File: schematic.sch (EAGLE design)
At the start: 31 parts, among them IC1 FT230XS, IC2 ATMEGA644A, IC4 L4931D, X1 MINI-USB-32005-301

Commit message: saving to git
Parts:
- added C11: .1uf, eagle-ltspice:CC0504
- added C12, C13, C17: 1uF, eagle-ltspice:CC0504
- added C14, C15: 2.2uF, eagle-ltspice:CC0504
- added C16: .1uF, eagle-ltspice:CC0504
- added R12, R13: 2K, eagle-ltspice:RR0603
- added R14: 390K, eagle-ltspice:RR0603
- added U$3: UG-2864HSWEG01, adafruit:UG-2864HSWEG01
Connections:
- new net N$10: C13.1, U$3.C2N
- new net N$11: C17.2, U$3.C1P
- new net N$12: C17.1, U$3.C1N
- new net N$5: C14.2, U$3.VCOMH
- new net N$7: C13.2, U$3.C2P
- new net N$9: R14.1, U$3.IREF
- new net OLED_SCL: R12.1, U$3.D0/DI
- new net OLED_SDA: R13.1, U$3.D1/SCLK, U$3.D2
- new net OLED_VCC: C15.2, C16.2, U$3.VCC
- new net OLED_VDD: C11.2, C12.2, R12.2, R13.2, U$3./RES, U$3.BS1, U$3.VBAT, U$3.VDD
- new net OLED_VSS: U$3./CS, U$3.BS0, U$3.BS2, U$3.R/W
- net GND: now also C11.1, C12.1, C14.1, C15.1, C16.1, R14.2, U$3.D/C, U$3.E/RD, U$3.VLSS, U$3.VSS
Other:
- moved on the sheet: X1

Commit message: saving
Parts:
- removed IC2: ATMEGA644A, atmel:ATMEGA644A
- added C18: 1uF, eagle-ltspice:CC0504
- added IC3: ATMEGA32U2-TQFP, adafruit:ATMEGA32U2-TQFP
- added JP1: (no value), adafruit:PINHD-1X6B
- added R15, R16: 22, eagle-ltspice:RR0603
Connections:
- new net N$13: IC3.PB3(PDO/MISO/PCINT3), JP1.4
- new net N$14: C18.2, IC3.UCAP
- new net N$15: IC3.D-, R15.1
- new net N$16: IC3.D+, R16.1
- new net N$3: IC3.PB1(SCK/PCINT1), JP1.2
- new net N$4: IC3.PB2(PDI/MOSI/PCINT2), JP1.3
- new net RESET: IC3./RESET(PC1), JP1.5
- new net UGND: IC3.UGND, X1.4
- new net VUSB: C1.1, U$1.CE, U$1.VDD, X1.1
- net B0: no longer IC2.(PCINT26/INT0)PD2
- net B1: no longer IC2.(PCINT27/INT1)PD3
- net B2: no longer IC2.(PCINT28/OC1B)PD4
- net GND: now also C18.1, IC3.GND, JP1.6, U$3.MT, U$3.MT2; no longer IC2.GND, IC2.GND@1, IC2.GND@2, IC2.GND@3, X1.4
- net OLED_VDD: no longer C11.2, C12.2, U$3.VBAT, U$3.VDD
- net USB+: now also R16.2
- net USB-: now also R15.2
- net VCC: now also C11.2, C12.2, IC3.VCC, JP1.1, U$3.VBAT, U$3.VDD; no longer IC2.VCC, IC2.VCC@1, IC2.VCC@2
- net VCHG: no longer C1.1, U$1.CE, U$1.VDD, X1.1
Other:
- moved on the sheet: SV1

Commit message: Saving to git
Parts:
- removed IC3: ATMEGA32U2-TQFP, adafruit:ATMEGA32U2-TQFP
- removed R15, R16: 22, eagle-ltspice:RR0603
- removed S1, S4, S5: (no value), switch-omron:10-XX
- removed SV1: (no value), con-lsta:FE05-1
- removed U$2: RN4020, microchip_bluetooth_v101:RN4020
- added JP2: (no value), pinhead:PINHD-1X2
- added JP3: (no value), adafruit:PINHD-1X3
- added LED1, LED2, LED3: (no value), adafruit:LEDSMT1206
- added R17, R18, R19: 2K, eagle-ltspice:RR0603
- added SW1, SW2, SW3: (no value), adafruit:SWITCH_PUSHBUTTONSOFTTOUCHSMD_SJ
- added U$4: ATMEGA32U4-AU, adafruit:ATMEGA32U4-AU
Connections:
- removed net 6: IC1.RXD, R9.2
- removed net N$15: IC3.D-, R15.1
- removed net N$16: IC3.D+, R16.1
- removed net VCHG: C7.1, L1.2, SV1.5
- new net N$17: LED1.A, R17.1
- new net N$18: LED2.A, R18.1
- new net N$19: LED3.A, R19.1
- new net N$21: R19.2, U$4.PB5(OC1A/ADC12/!OC4B)
- new net N$22: R18.2, U$4.PB6(OC1B/OC4B/ADC13)
- new net N$23: R17.2, U$4.PB7(OC0A/OC1C/RTS)
- new net RXD: IC1.RXD, JP2.2, R9.2, U$4.PD2(INT2/RXD1)
- net B0: now also SW1.P$2, U$4.PD4(ICP1/ADC8); no longer S1.S1
- net B1: now also SW2.P$2, U$4.PD5(XCK/CTS); no longer S4.S1
- net B2: now also SW3.P$2, U$4.PD6(T1/ADC9/!OC4D); no longer S5.S1
- net GND: now also JP3.3, LED1.C, LED2.C, LED3.C, U$4.GND, U$4.GND1, U$4.GND2, U$4.GND3; no longer IC3.GND, SV1.3
- net N$13: now also U$4.PB1(SCK); no longer IC3.PB3(PDO/MISO/PCINT3)
- net N$14: now also U$4.UCAP; no longer IC3.UCAP
- net N$3: now also U$4.PB3(PDO/MISO); no longer IC3.PB1(SCK/PCINT1)
- net N$4: now also U$4.PB2(PDI/MOSI); no longer IC3.PB2(PDI/MOSI/PCINT2)
- net OLED_SCL: now also U$4.PD0(INT0/OC0B/SCL)
- net OLED_SDA: now also U$4.PD1(INT1/SDA)
- net RESET: now also U$4./RESET; no longer IC3./RESET(PC1)
- net TXD: now also JP2.1, U$4.PD3(INT3/TXD1)
- net UGND: now also U$4.UGND; no longer IC3.UGND
- net USB+: no longer R16.2
- net USB-: no longer R15.2
- net VBAT+: now also JP3.2; no longer SV1.4
- net VCC: now also C7.1, L1.2, SW1.P$1, SW2.P$1, SW3.P$1, U$4.AVCC, U$4.AVCC1, U$4.VCC, U$4.VCC1; no longer IC3.VCC, S1.P, S4.P, S5.P
- net VUSB: now also JP3.1, U$4.UVCC, U$4.VBUS
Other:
- moved on the sheet: JP1

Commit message: Finished layout V1
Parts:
- removed JP2: (no value), pinhead:PINHD-1X2
- added JP4, JP5: (no value), adafruit:PINHD-1X1
- R17, R18, R19: value 2K -> 330
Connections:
- net 2 renamed 9
- net 3 renamed 8
- removed net N$13: JP1.4, U$4.PB1(SCK)
- removed net N$3: JP1.2, U$4.PB3(PDO/MISO)
- removed net N$4: JP1.3, U$4.PB2(PDI/MOSI)
- removed net OLED_VCC: C15.2, C16.2, U$3.VCC
- removed net OLED_VSS: U$3./CS, U$3.BS0, U$3.BS2, U$3.R/W
- removed net UGND: U$4.UGND, X1.4
- new net FTDI_VCC: IC1.VCC, L1.1
- new net MISO: JP1.3, U$4.PB3(PDO/MISO)
- new net MOSI: JP1.4, U$4.PB2(PDI/MOSI)
- new net SCK: JP1.5, U$4.PB1(SCK)
- net GND: now also U$3./CS, U$3.BS0, U$3.BS2, U$3.R/W, U$4.UGND, X1.4
- net OLED_VDD: no longer U$3./RES, U$3.BS1
- net RESET: now also JP1.2; no longer JP1.5
- net RXD: now also JP5.1; no longer JP2.2
- net TXD: now also JP4.1; no longer JP2.1
- net VCC: now also C15.2, C16.2, U$3./RES, U$3.BS1, U$3.VCC; no longer IC1.VCC, L1.1

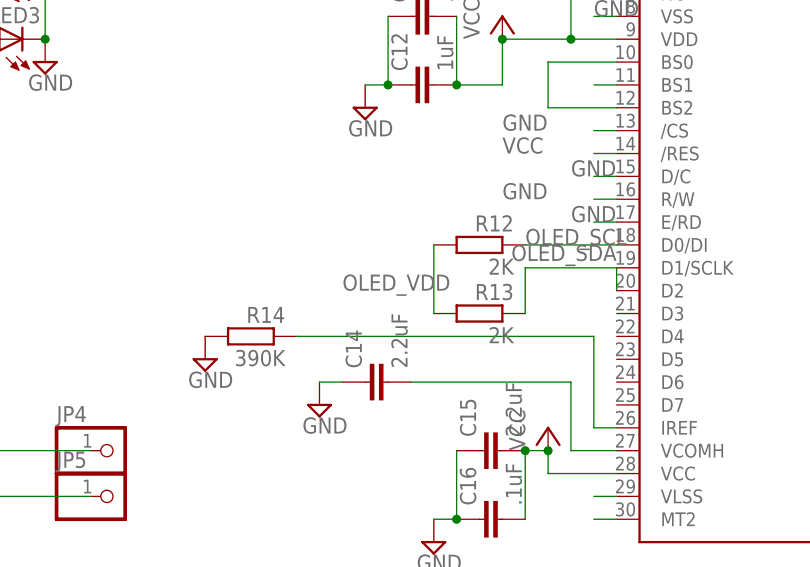
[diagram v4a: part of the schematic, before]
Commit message: Checked and fixed with OSH Park DRC
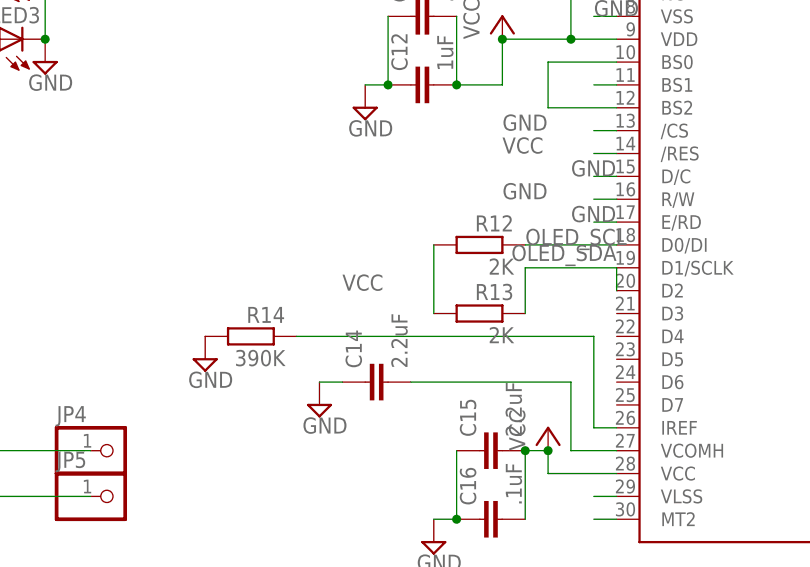
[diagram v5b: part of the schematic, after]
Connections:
- removed net OLED_VDD: R12.2, R13.2
- net VCC: now also R12.2, R13.2
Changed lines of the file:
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@@
 <wire x1="55.88" y1="43.18" x2="53.34" y2="43.18" width="0.1524" layer="91"/>
+</segment>
+<segment>
+<pinref part="R12" gate="G$1" pin="2"/>
+<pinref part="R13" gate="G$1" pin="2"/>
+<wire x1="35.56" y1="25.4" x2="35.56" y2="17.78" width="0.1524" layer="91"/>
+<label x="25.4" y="20.32" size="1.778" layer="95"/>
 </segment>
 </net>
@@
 </segment>
 </net>
-<net name="OLED_VDD" class="0">
-<segment>
-<pinref part="R12" gate="G$1" pin="2"/>
-<pinref part="R13" gate="G$1" pin="2"/>
-<wire x1="35.56" y1="25.4" x2="35.56" y2="17.78" width="0.1524" layer="91"/>
-<label x="25.4" y="20.32" size="1.778" layer="95"/>
-</segment>
-</net>

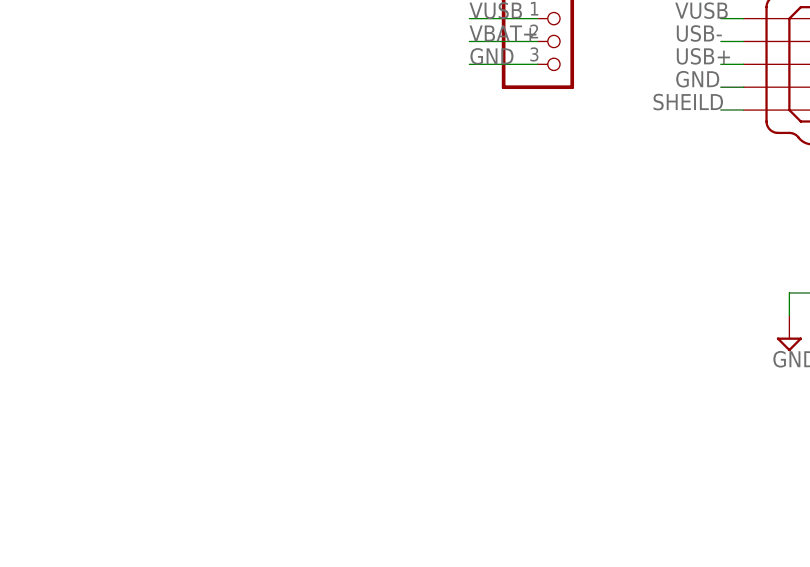
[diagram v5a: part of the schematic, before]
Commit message: Added Power LED, passed DRC
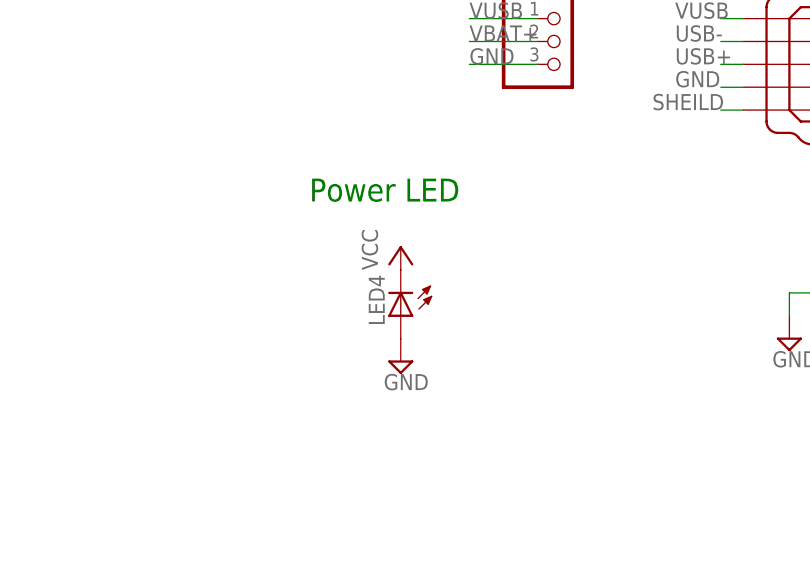
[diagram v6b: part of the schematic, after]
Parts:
- added LED4: (no value), adafruit:LEDSMT1206
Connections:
- net GND: now also LED4.A
- net VCC: now also LED4.C
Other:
- note added: "Power LED"
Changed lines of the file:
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@@
 <part name="JP4" library="adafruit" deviceset="PINHD-1X1" device=""/>
 <part name="JP5" library="adafruit" deviceset="PINHD-1X1" device=""/>
+<part name="P+4" library="supply1" deviceset="VCC" device=""/>
+<part name="LED4" library="adafruit" deviceset="LED" device="SMT1206"/>
+<part name="SUPPLY19" library="supply2" deviceset="GND" device=""/>
 </parts>
 <sheets>
@@
 <text x="40.64" y="142.24" size="2.54" layer="91">USB to Serial Converter</text>
 <wire x1="20.32" y1="81.28" x2="121.92" y2="81.28" width="1.27" layer="98"/>
+<text x="-172.72" y="43.18" size="2.54" layer="91">Power LED</text>
 </plain>
 <instances>
@@
 <instance part="JP4" gate="G$1" x="0" y="2.54"/>
 <instance part="JP5" gate="G$1" x="0" y="-2.54"/>
+<instance part="P+4" gate="VCC" x="-162.56" y="38.1"/>
+<instance part="LED4" gate="G$1" x="-162.56" y="30.48" rot="R180"/>
+<instance part="SUPPLY19" gate="GND" x="-162.56" y="25.4"/>
 </instances>
 <busses>
@@
 <pinref part="U$3" gate="G$1" pin="BS2"/>
 <wire x1="55.88" y1="40.64" x2="48.26" y2="40.64" width="0.1524" layer="91"/>
+</segment>
+<segment>
+<pinref part="LED4" gate="G$1" pin="A"/>
+<pinref part="SUPPLY19" gate="GND" pin="GND"/>
 </segment>
 </net>
@@
 <label x="25.4" y="20.32" size="1.778" layer="95"/>
 </segment>
+<segment>
+<pinref part="P+4" gate="VCC" pin="VCC"/>
+<pinref part="LED4" gate="G$1" pin="C"/>
+</segment>
 </net>
